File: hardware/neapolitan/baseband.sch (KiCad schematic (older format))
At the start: 73 parts, among them P14 XCVR_CLKOUT, P15 INTR, P18 OEB, P36 VAA, P39 SSP0_SCK, P40 SSP0_MOSI, P41 SSP0_MISO, P53 CS_XCVR, P55 TXENABLE, P56 RXENABLE, P57 XTAL2, P67 RSSI, P83 GND, P84 GND, P85 GND, P86 GND, P87 GND, P88 GND, P89 GND, P9 BASEBAND, P90 GND, P91 GND, P92 GND, Q3 MOSFET_P, T3 RX_BALUN, T4 TX_BALUN, U17 MAX2837, U19 SI5351C, X1 GSG-XTAL4PIN

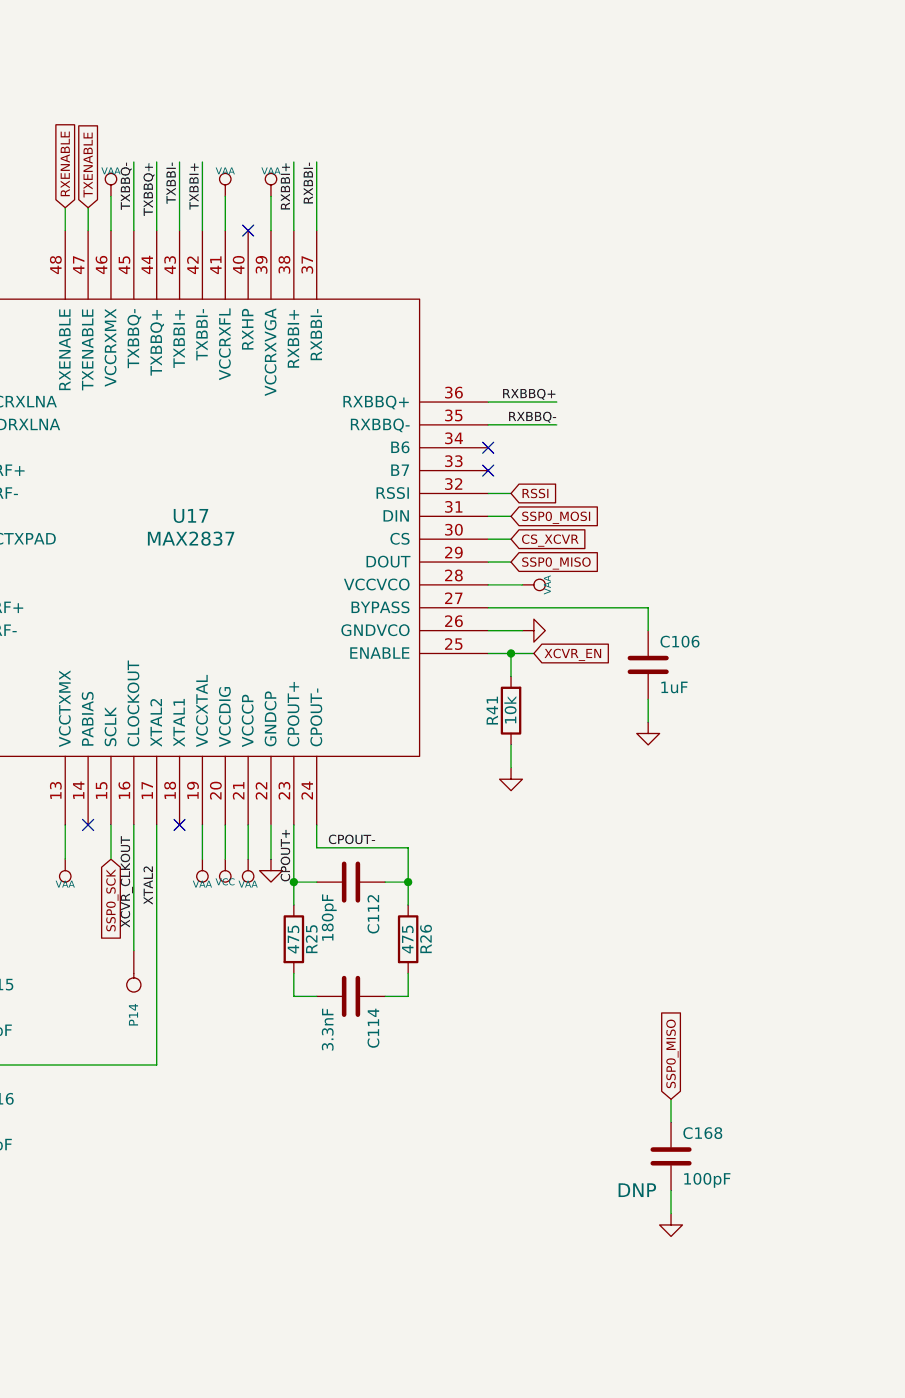
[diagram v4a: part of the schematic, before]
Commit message: Neapolitan: completed initial layout
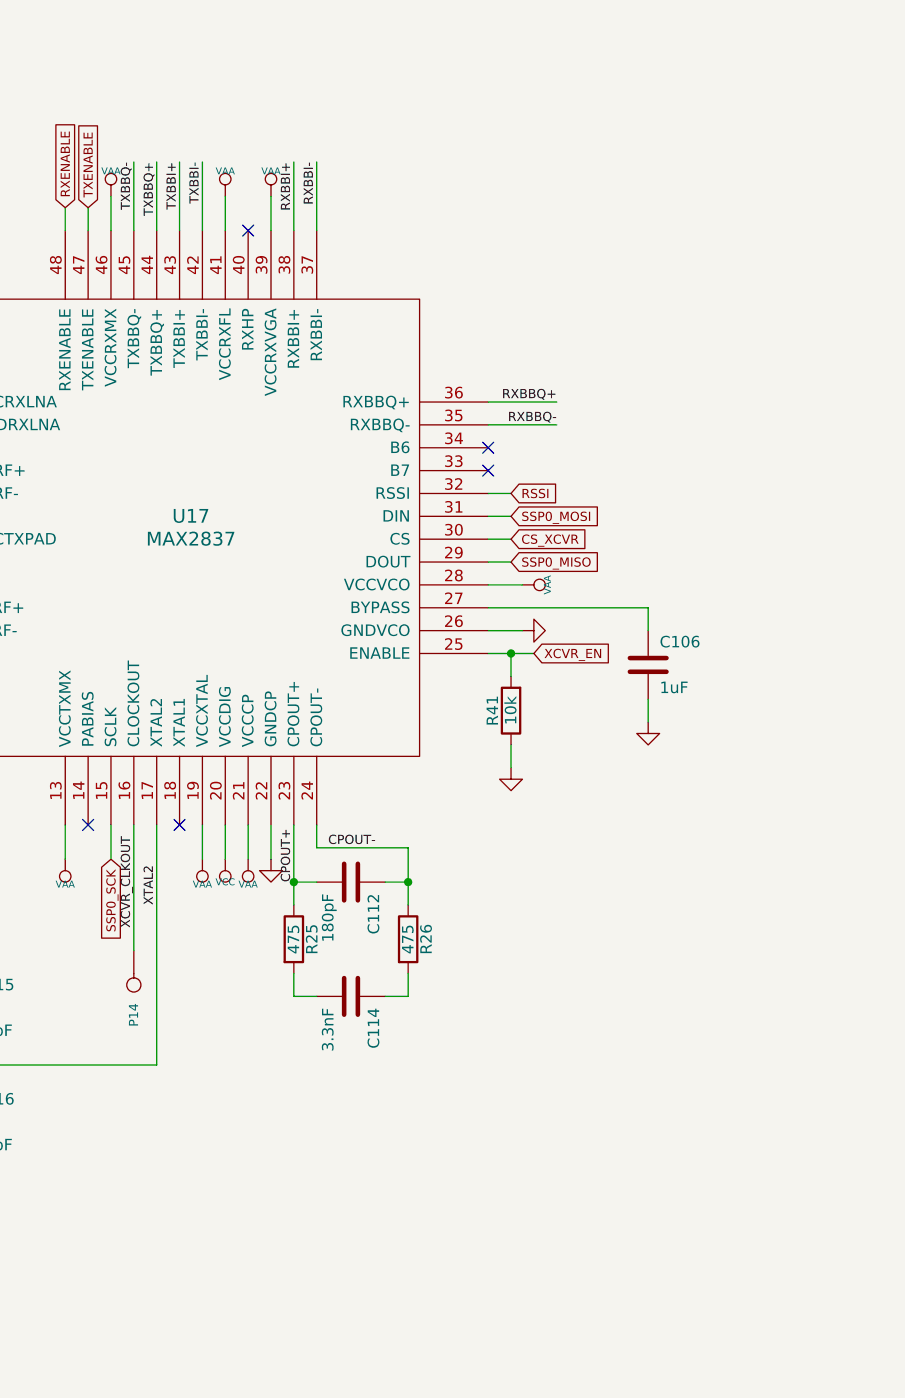
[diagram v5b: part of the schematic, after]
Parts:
- removed C168: 100pF, hackrf:GSG-0402, symbol C
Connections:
- net TXBBI+: now also U17.43 (TXBBI+); no longer U17.42 (TXBBI-)
- net TXBBI-: now also U17.42 (TXBBI-); no longer U17.43 (TXBBI+)
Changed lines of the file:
@@
 Text Label 8150 3350 3    40   ~ 0
 RXBBI+
+Text Label 7750 3350 3    40   ~ 0
+TXBBI-
 Text Label 7650 3350 3    40   ~ 0
-TXBBI-
-Text Label 7750 3350 3    40   ~ 0
 TXBBI+
 Text Label 7550 3350 3    40   ~ 0
@@
 	1    0    0    -1
 $EndComp
-Text GLabel 9800 7450 1    40   Input ~ 0
-SSP0_MISO
-$Comp
-L C C168
-U 1 1 52963CCA
-P 9800 7700
-F 0 "C168" H 9850 7800 50  0000 L CNN
-F 1 "100pF" H 9850 7600 50  0000 L CNN
-F 2 "hackrf:GSG-0402" H 9800 7700 60  0001 C CNN
-F 3 "" H 9800 7700 60  0001 C CNN
-F 4 "Murata" H 9800 7700 60  0001 C CNN "Manufacturer"
-F 5 "GRM1555C1H101JA01D" H 9800 7700 60  0001 C CNN "Part Number"
-F 6 "CAP CER 100PF 50V 5% NP0 0402" H 9800 7700 60  0001 C CNN "Description"
-F 7 "DNP" H 9650 7550 60  0000 C CNN "Note"
-	1    9800 7700
-	1    0    0    -1
-$EndComp
-$Comp
-L GND #PWR0149
-U 1 1 52963CD7
-P 9800 7950
-F 0 "#PWR0149" H 9800 7950 30  0001 C CNN
-F 1 "GND" H 9800 7880 30  0001 C CNN
-F 2 "" H 9800 7950 60  0000 C CNN
-F 3 "" H 9800 7950 60  0000 C CNN
-	1    9800 7950
-	1    0    0    -1
-$EndComp
 $Comp
 L C C169
@@
 $EndComp
 $Comp
-L GND #PWR0150
+L GND #PWR0149
 U 1 1 52AA563D
 P 2750 6800
-F 0 "#PWR0150" H 2750 6800 30  0001 C CNN
+F 0 "#PWR0149" H 2750 6800 30  0001 C CNN
 F 1 "GND" H 2750 6730 30  0001 C CNN
 F 2 "" H 2750 6800 60  0000 C CNN
@@
 $EndComp
 $Comp
-L GND #PWR0151
+L GND #PWR0150
 U 1 1 52AA564A
 P 3350 6800
-F 0 "#PWR0151" H 3350 6800 30  0001 C CNN
+F 0 "#PWR0150" H 3350 6800 30  0001 C CNN
 F 1 "GND" H 3350 6730 30  0001 C CNN
 F 2 "" H 3350 6800 60  0000 C CNN
@@
 Connection ~ 11300 8300
 Wire Wire Line
-	9800 7950 9800 7850
-Wire Wire Line
-	9800 7550 9800 7450
-Wire Wire Line
 	3350 6800 3350 6900

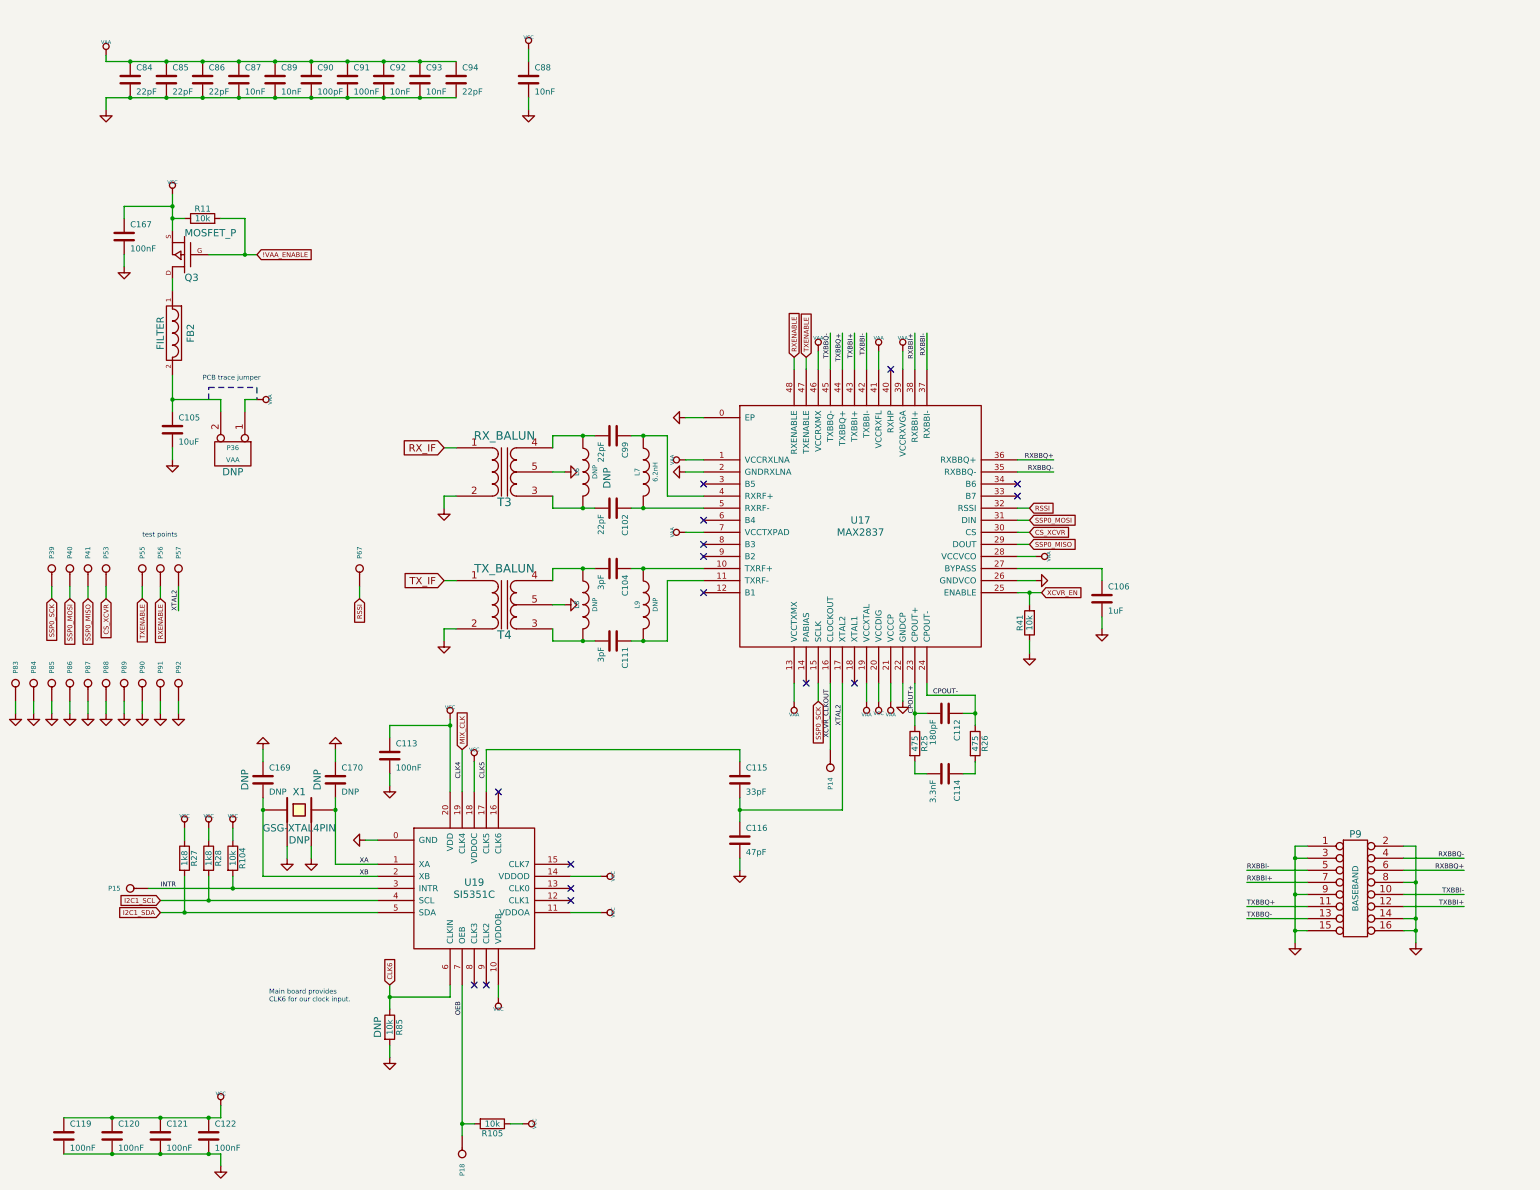
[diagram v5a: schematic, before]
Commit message: Neapolitan: added RF chokes to some supply pins as a noise reduction experiment
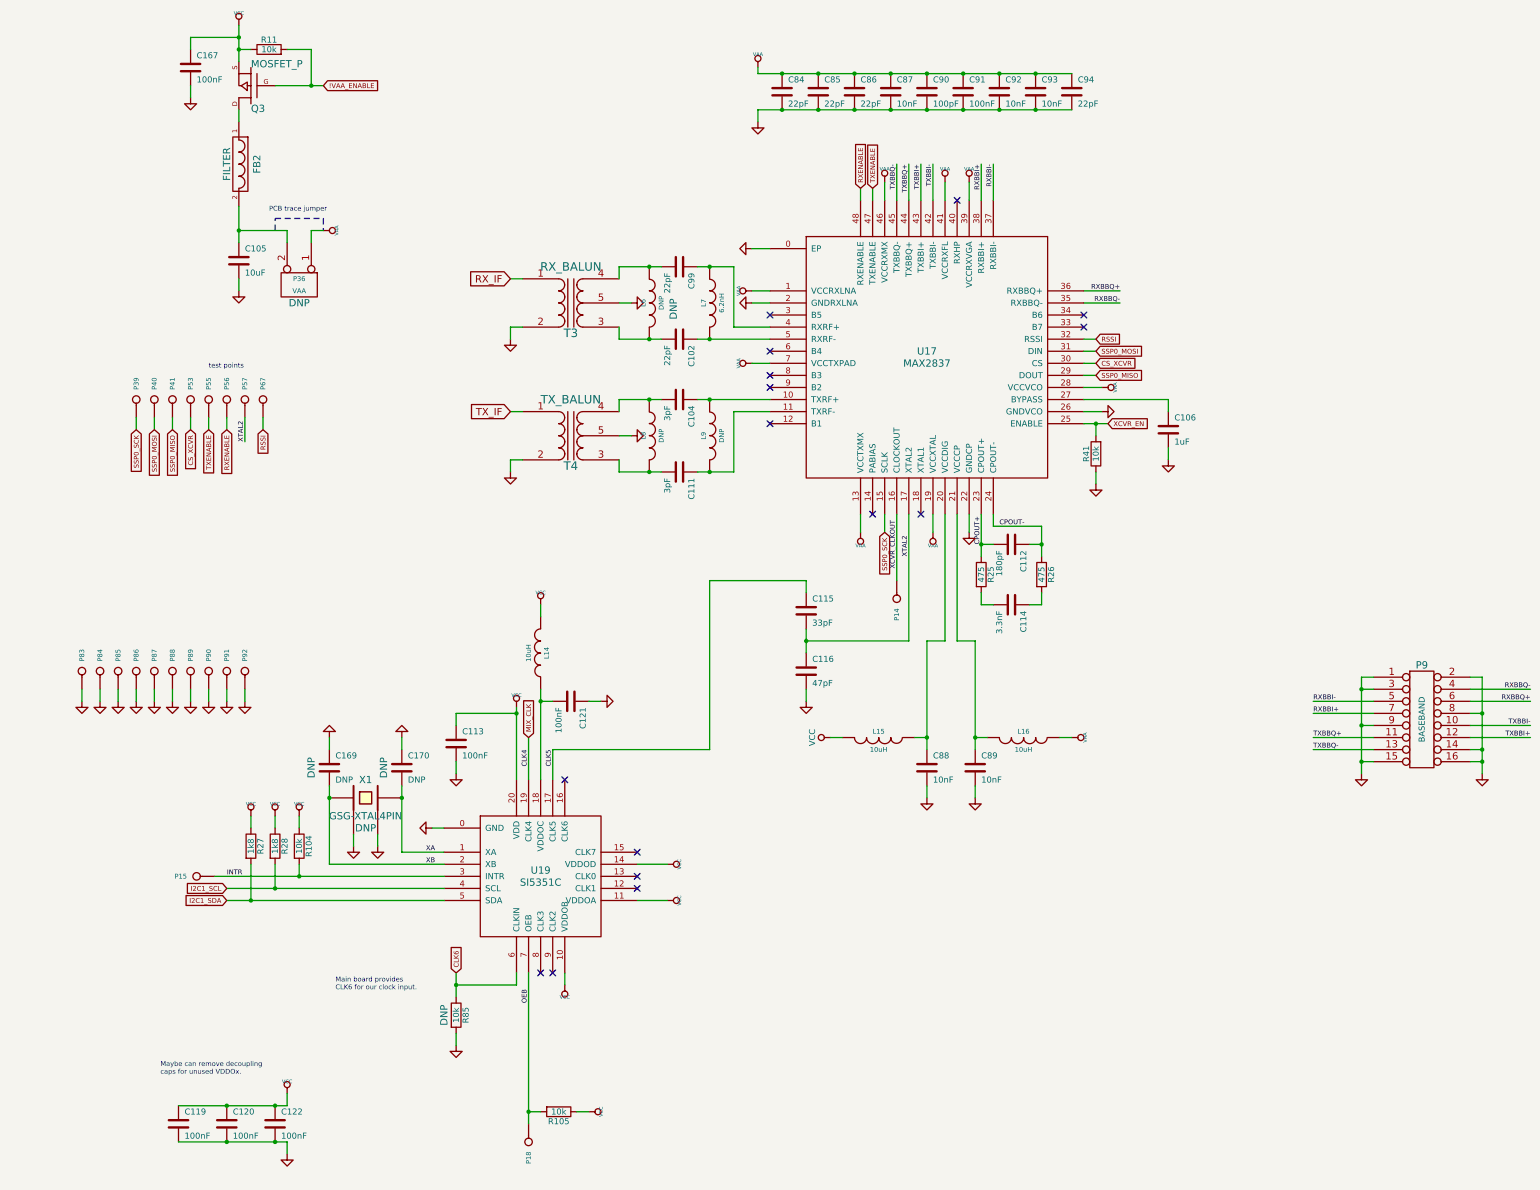
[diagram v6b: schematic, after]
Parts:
- added L14, L15, L16: 10uH, hackrf:GSG-0603, symbol INDUCTOR
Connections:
- net GND: now also C121.1; no longer C121.2
- net VAA: now also L16.1; no longer C89.1, U17.21 (VCCCP)
- net VCC: now also L14.2, L15.2; no longer C121.1, C88.1, U17.20 (VCCDIG), U19.18 (VDDOC)
- new net: C88.1, L15.1, U17.20 (VCCDIG)
- new net: C89.1, L16.2, U17.21 (VCCCP)
- new net: C121.2, L14.1, U19.18 (VDDOC)
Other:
- note added: "Maybe can remove decoupling\ncaps for unused VDDOx."
- moved on the sheet: C102, C104, C105, C106, C111, C112, C113, C114, C115, C116, C119, C120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

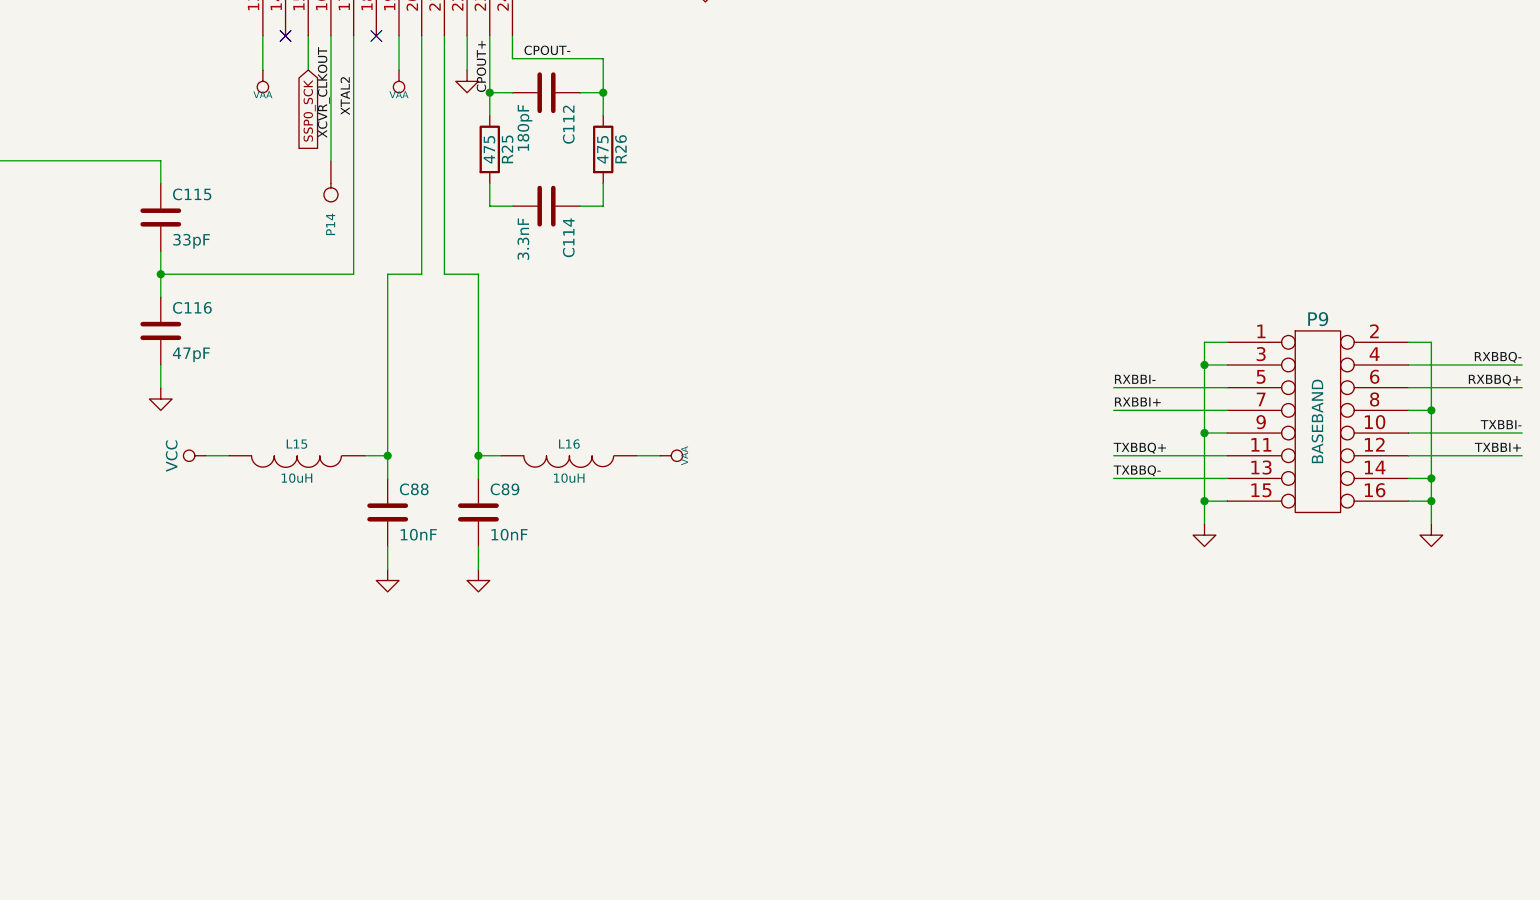
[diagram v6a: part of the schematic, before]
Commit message: Neapolitan: added decoupling caps near pin headers
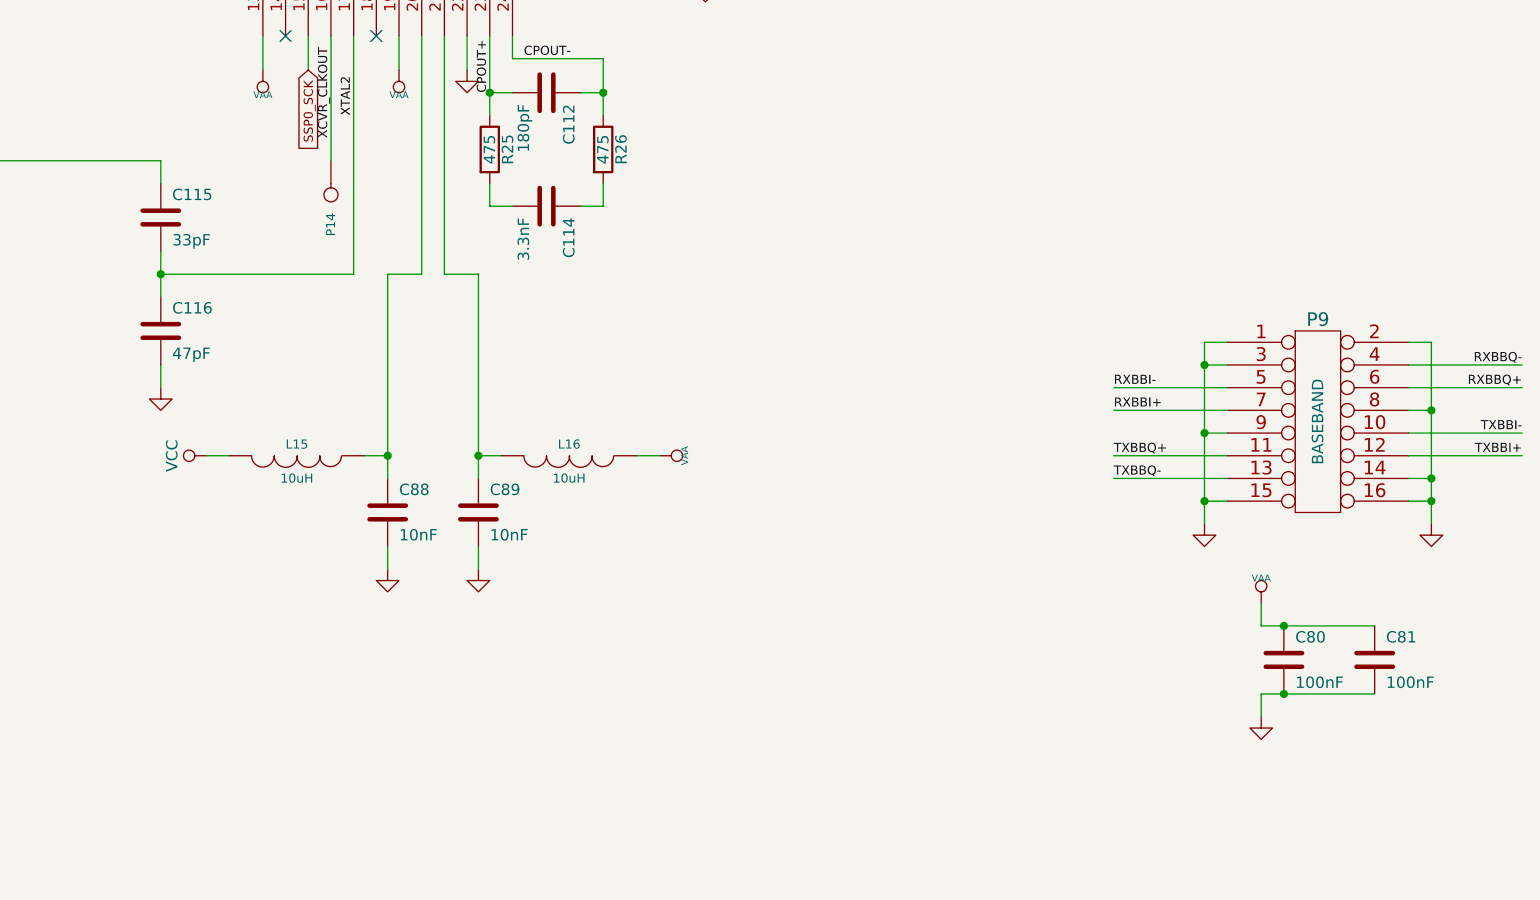
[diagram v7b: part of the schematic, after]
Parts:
- added C80, C81: 100nF, hackrf:GSG-0402, symbol C
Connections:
- net GND: now also C80.2, C81.2
- net VAA: now also C80.1, C81.1
